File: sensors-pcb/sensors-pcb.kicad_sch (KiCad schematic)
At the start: 0 parts

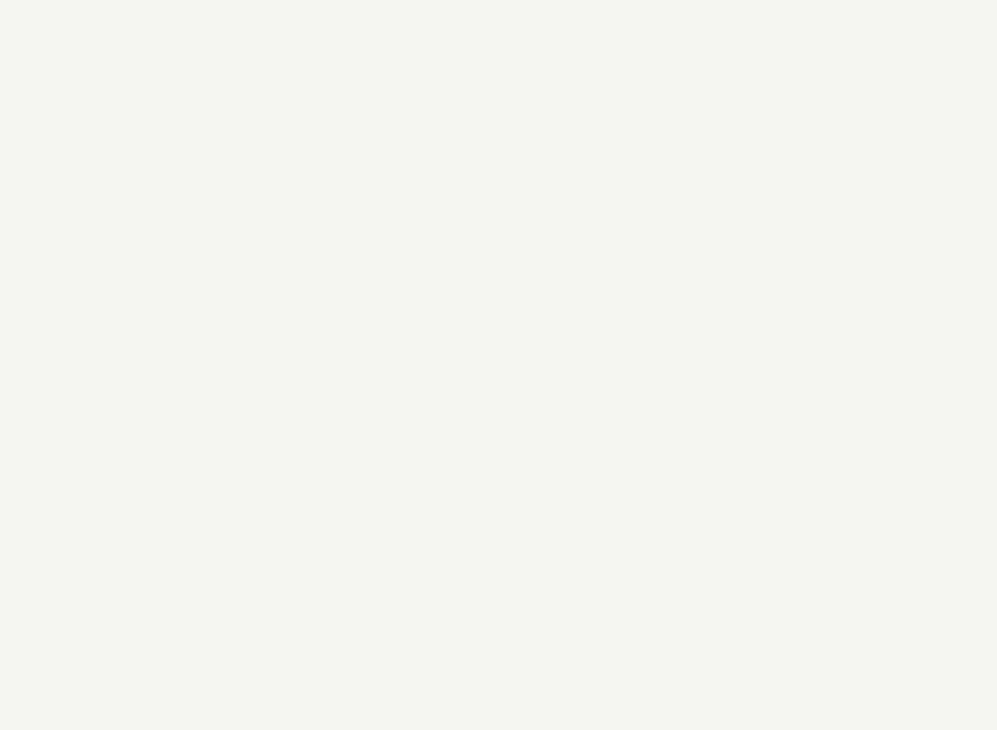
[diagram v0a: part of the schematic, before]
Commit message: Ajusté symbole IMU et commencé schéma
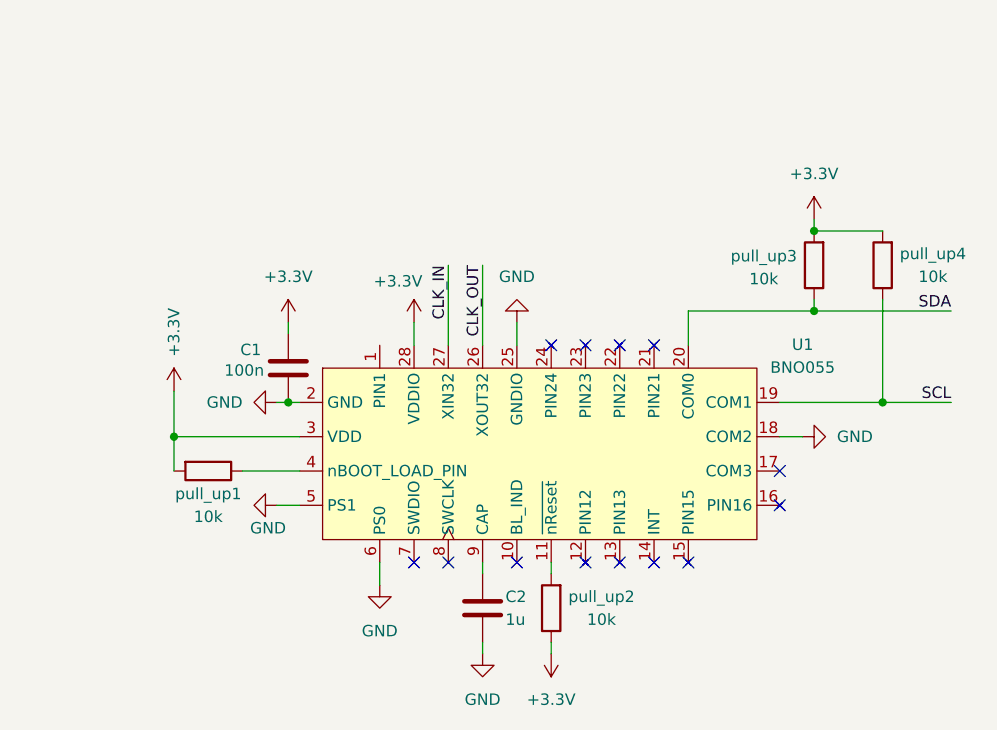
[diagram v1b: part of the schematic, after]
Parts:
- added C1: 100n, symbol Device:C
- added C2: 1u, symbol Device:C
- added U1: BNO055, symbol Exocet:BNO055
- added pull_up1, pull_up2, pull_up3, pull_up4: 10k, symbol Device:R
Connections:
- new net: C2.1, U1.9 (CAP)
- new net: U1.11 (~{nReset}), pull_up2.2
- new net: U1.4 (nBOOT_LOAD_PIN), pull_up1.1
- new net +3.3V: C1.2, U1.28 (VDDIO), U1.3 (VDD), pull_up1.2, pull_up2.1, pull_up3.2, pull_up4.2
- new net CLK_IN: U1.27 (XIN32)
- new net CLK_OUT: U1.26 (XOUT32)
- new net GND: C1.1, C2.2, U1.18 (COM2), U1.2 (GND), U1.25 (GNDIO), U1.5 (PS1), U1.6 (PS0)
- new net SCL: U1.19 (COM1), pull_up4.1
- new net SDA: U1.20 (COM0), pull_up3.1
- no-connect marks 0 -> 13

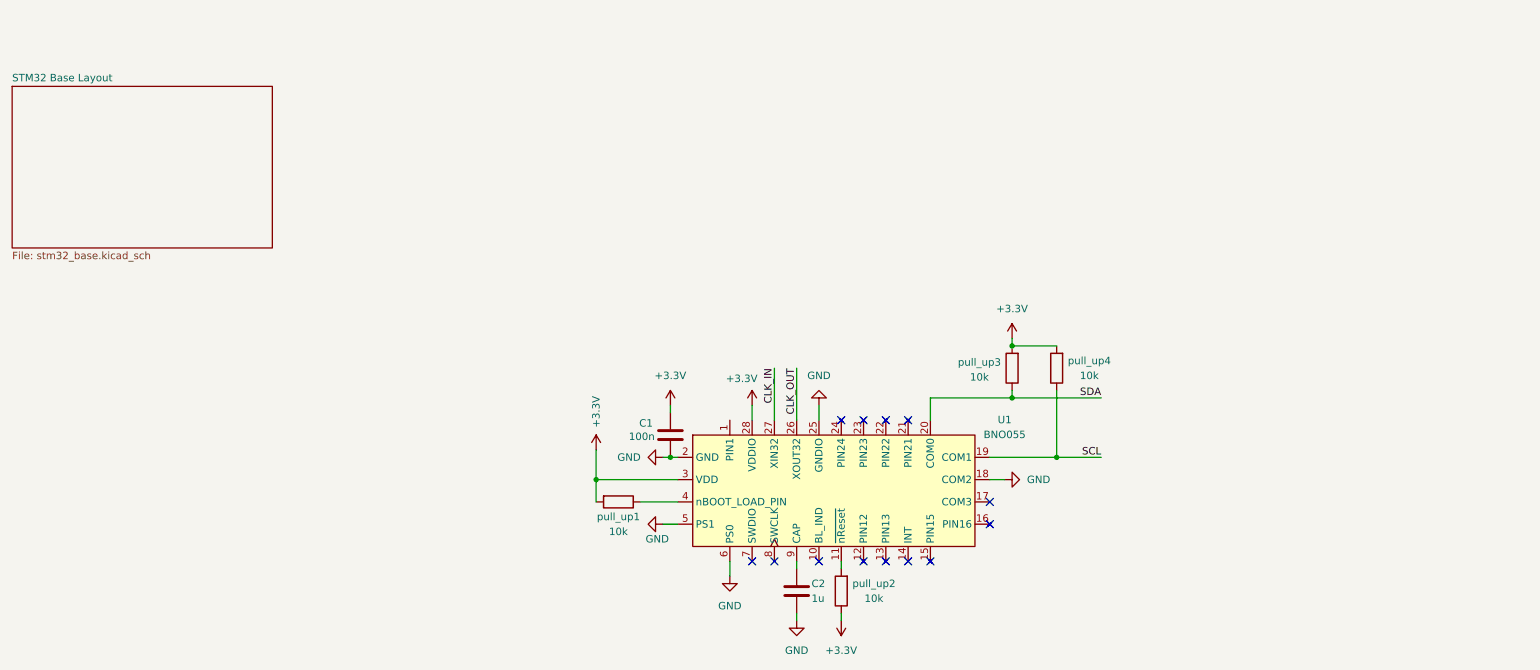
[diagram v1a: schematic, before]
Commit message: sensors-pcb: adjust IMU schematic and symbol
hide no connect pins
add connect I2C I/O to STM32 with pull-up resistors
add external 42kHz clock from Exocet template
pins 15 and 16 connected to GND through solder jumper
because of conflicting datasheet info (2021 vs 2016). to be tested IRL
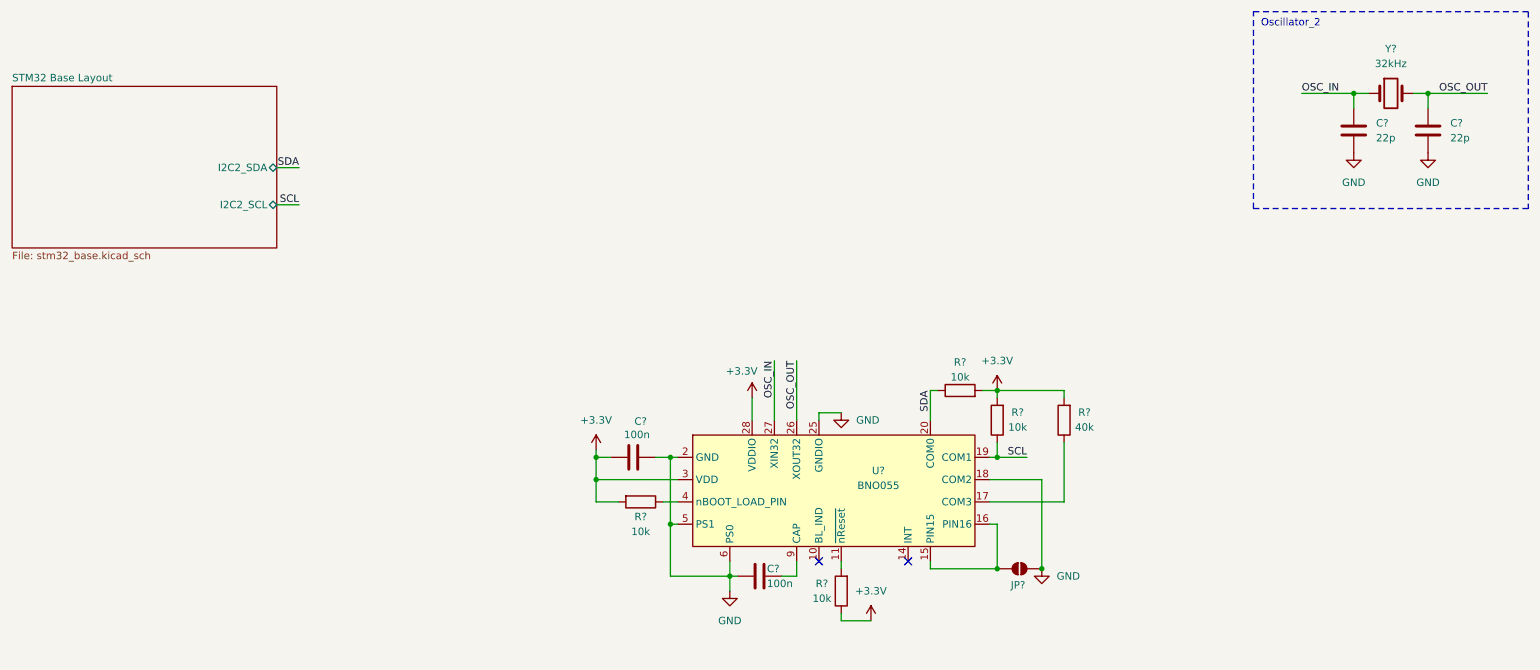
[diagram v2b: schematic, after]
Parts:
- removed pull_up3: 10k, symbol Device:R
- added C? (x2): 22p, Capacitor_SMD:C_0603_1608Metric, symbol Device:C
- added JP?: SolderJumper_2_Open, symbol Jumper:SolderJumper_2_Open
- added R?: 40k, symbol Device:R
- added R?: 10k, symbol Device:R
- added Y?: 32kHz, Exocet:Crystal_SMD_HC49-SD, symbol Exocet:HSE_Oscillator
- C?: renamed from C2; value 1u -> 100n
- renumbered C1 to C?, pull_up2 to R?, pull_up4 to R?, pull_up1 to R?, U1 to U?
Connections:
- net +3.3V: now also C?.1, R?.2, R?.2; no longer C?.2
- net GND: now also C?.2, C?.2, C?.2, JP?.2 (B); no longer C?.1
- net SDA: now also R?.1
- net at U?.15 (PIN15): now also U?.16 (PIN16), JP?.1 (A)
- net at U?.17 (COM3): now also R?.1
- net CLK_IN renamed OSC_IN
- net OSC_IN: now also C?.1, Y?.1
- net CLK_OUT renamed OSC_OUT
- net OSC_OUT: now also C?.1, Y?.2
- no-connect marks 13 -> 2
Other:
- sheet STM32 Base Layout ports: added I2C2_SCL, I2C2_SDA; removed none
- note added: "Oscillator_2"
- moved on the sheet: C?, R?

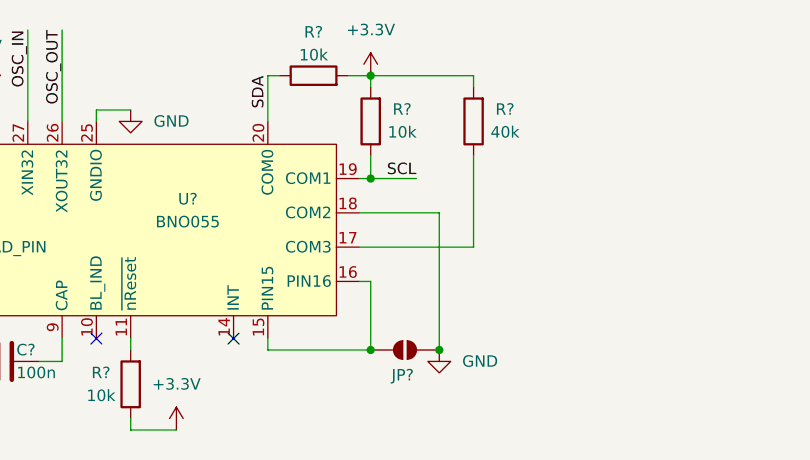
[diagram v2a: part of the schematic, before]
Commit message: sensors-pcb: add second solder junction
in case connecting pins together is illegal
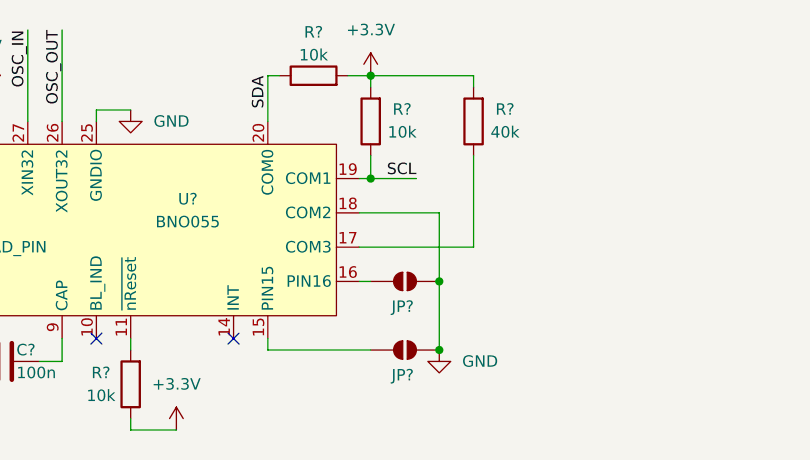
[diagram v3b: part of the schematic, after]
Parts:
- added JP?: SolderJumper_2_Open, symbol Jumper:SolderJumper_2_Open
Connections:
- net GND: now also JP?.2 (B)
- net at JP?.1 (A), U?.15 (PIN15): no longer U?.16 (PIN16)
- new net: JP?.1 (A), U?.16 (PIN16)
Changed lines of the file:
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@@
+	)
+	(junction
+		(at 200.66 100.33)
+		(diameter 0)
+		(color 0 0 0 0)
 	)
 	(junction
@@
 	(junction
 		(at 266.7 26.67)
-		(diameter 0)
-		(color 0 0 0 0)
-	)
-	(junction
-		(at 193.04 107.95)
 		(diameter 0)
 		(color 0 0 0 0)
@@
 	(wire
 		(pts
-			(xy 193.04 107.95) (xy 193.04 100.33)
-		)
-		(stroke
-			(width 0)
-			(type default)
-		)
-	)
-	(wire
-		(pts
 			(xy 147.32 109.22) (xy 147.32 111.76)
 		)
@@
 	(wire
 		(pts
+			(xy 200.66 100.33) (xy 200.66 107.95)
+		)
+		(stroke
+			(width 0)
+			(type default)
+		)
+	)
+	(wire
+		(pts
 			(xy 147.32 109.22) (xy 148.59 109.22)
 		)
@@
 	(wire
 		(pts
-			(xy 200.66 92.71) (xy 200.66 107.95)
+			(xy 200.66 92.71) (xy 200.66 100.33)
 		)
 		(stroke
@@
 					(unit 1)
 				)
+			)
+		)
+	)
+	(symbol
+		(lib_id "Jumper:SolderJumper_2_Open")
+		(at 196.85 100.33 0)
+		(unit 1)
+		(exclude_from_sim no)
+		(in_bom no)
+		(on_board yes)
+		(dnp no)
+		(property "Reference" "JP?"
+			(at 196.596 103.124 0)
+			(effects
+				(font
+					(size 1.27 1.27)
+				)
+			)
+		)
+		(property "Value" "SolderJumper_2_Open"
+			(at 196.596 105.664 0)
+			(effects
+				(font
+					(size 1.27 1.27)
+				)
+				(hide yes)
+			)
+		)
+		(property "Footprint" ""
+			(at 196.85 100.33 0)
+			(effects
+				(font
+					(size 1.27 1.27)
+				)
+				(hide yes)
+			)
+		)
+		(property "Datasheet" "~"
+			(at 196.85 100.33 0)
+			(effects
+				(font
+					(size 1.27 1.27)
+				)
+				(hide yes)
+			)
+		)
+		(property "Description" "Solder Jumper, 2-pole, open"
+			(at 196.85 100.33 0)
+			(effects
+				(font
+					(size 1.27 1.27)
+				)
+				(hide yes)
+			)
+		)
+		(pin "1"
+		)
+		(pin "2"
+		)
+		(instances
+			(project "sensors-pcb"
+				(path "/4b4cf3aa-c94c-4150-b9c5-35049cd71136"
+					(reference "JP?")
+					(unit 1)
+				)

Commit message: Symbole GPS
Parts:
- added AE1: Antenna, symbol Device:Antenna
- added R1, R2: 10k, symbol Device:R
- added R3: 50, symbol Device:R
- added U1: MAX-M8Q, RF_GPS:ublox_MAX, symbol RF_GPS:MAX-M8Q
- added V1: VPULSE, symbol Simulation_SPICE:VPULSE
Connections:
- net +3.3V: now also U1.14 (VCC_RF), U1.6 (V_BCKP), U1.7 (VCC_IO), U1.8 (VCC)
- net GND: now also U1.1 (GND), U1.10 (GND), U1.12 (GND), V1.2
- new net: AE1.1 (A), R3.1
- new net: U1.4 (TIMEPULSE), V1.1
- new net: R3.2, U1.11 (RF_IN)
- new net: R1.2, U1.16 (SDA)
- new net: R2.2, U1.17 (SCL)

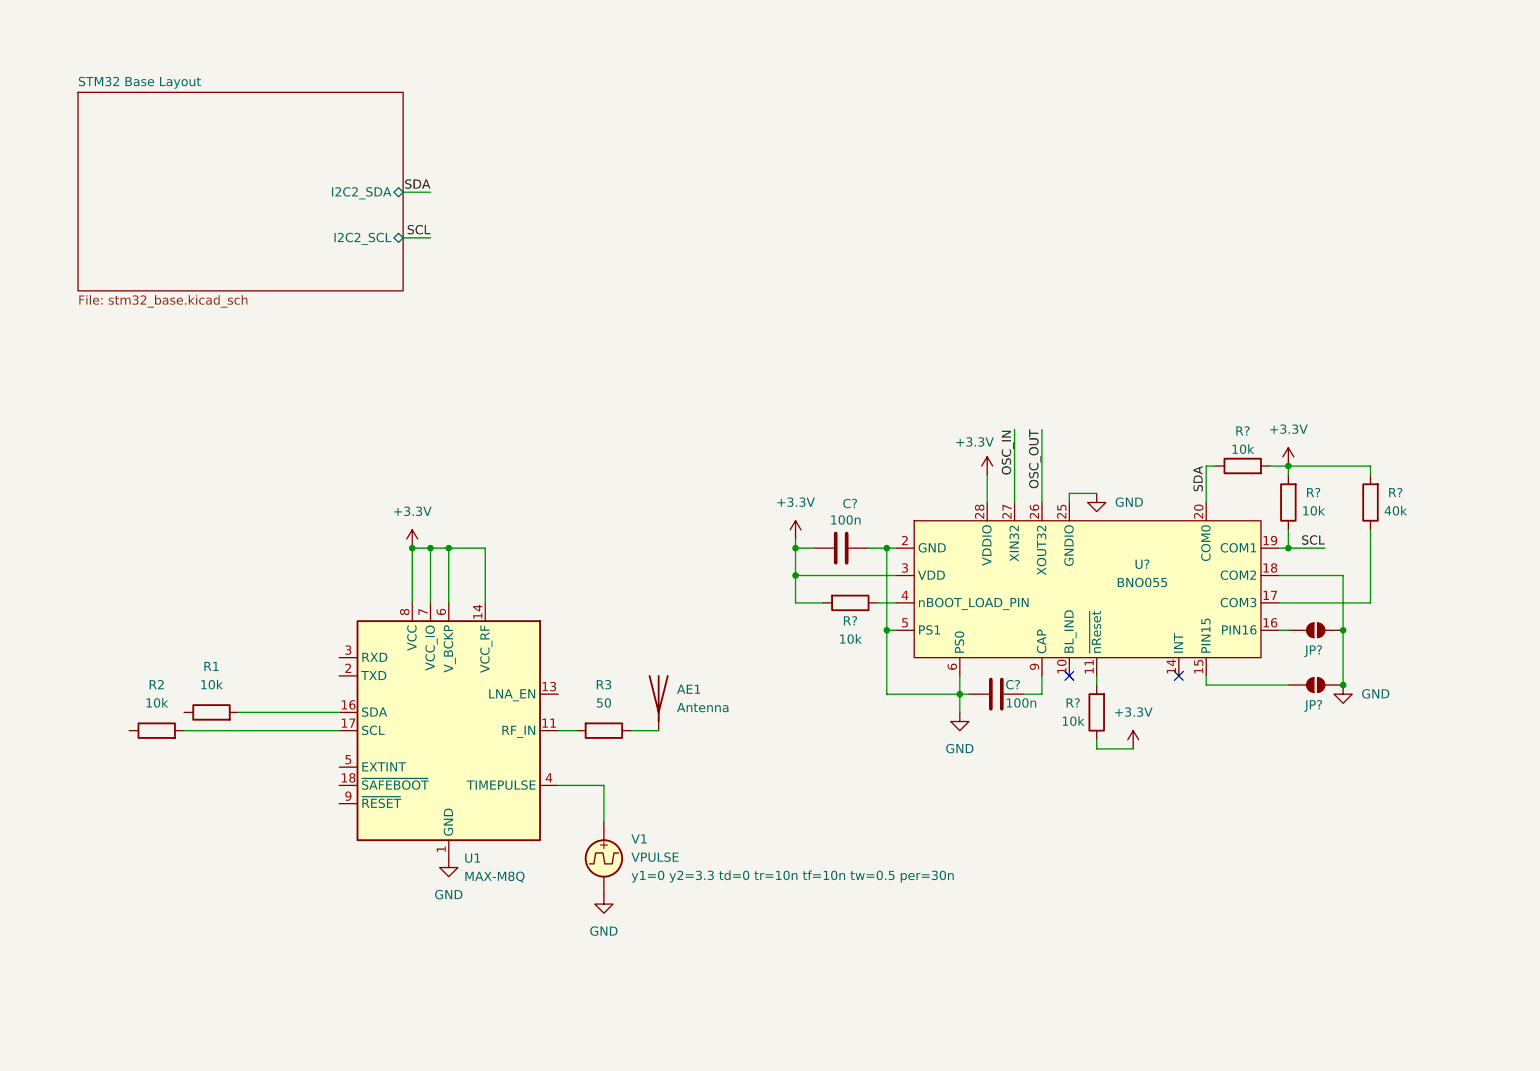
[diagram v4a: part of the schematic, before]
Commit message: sensors-pcb: finish GPS schematic
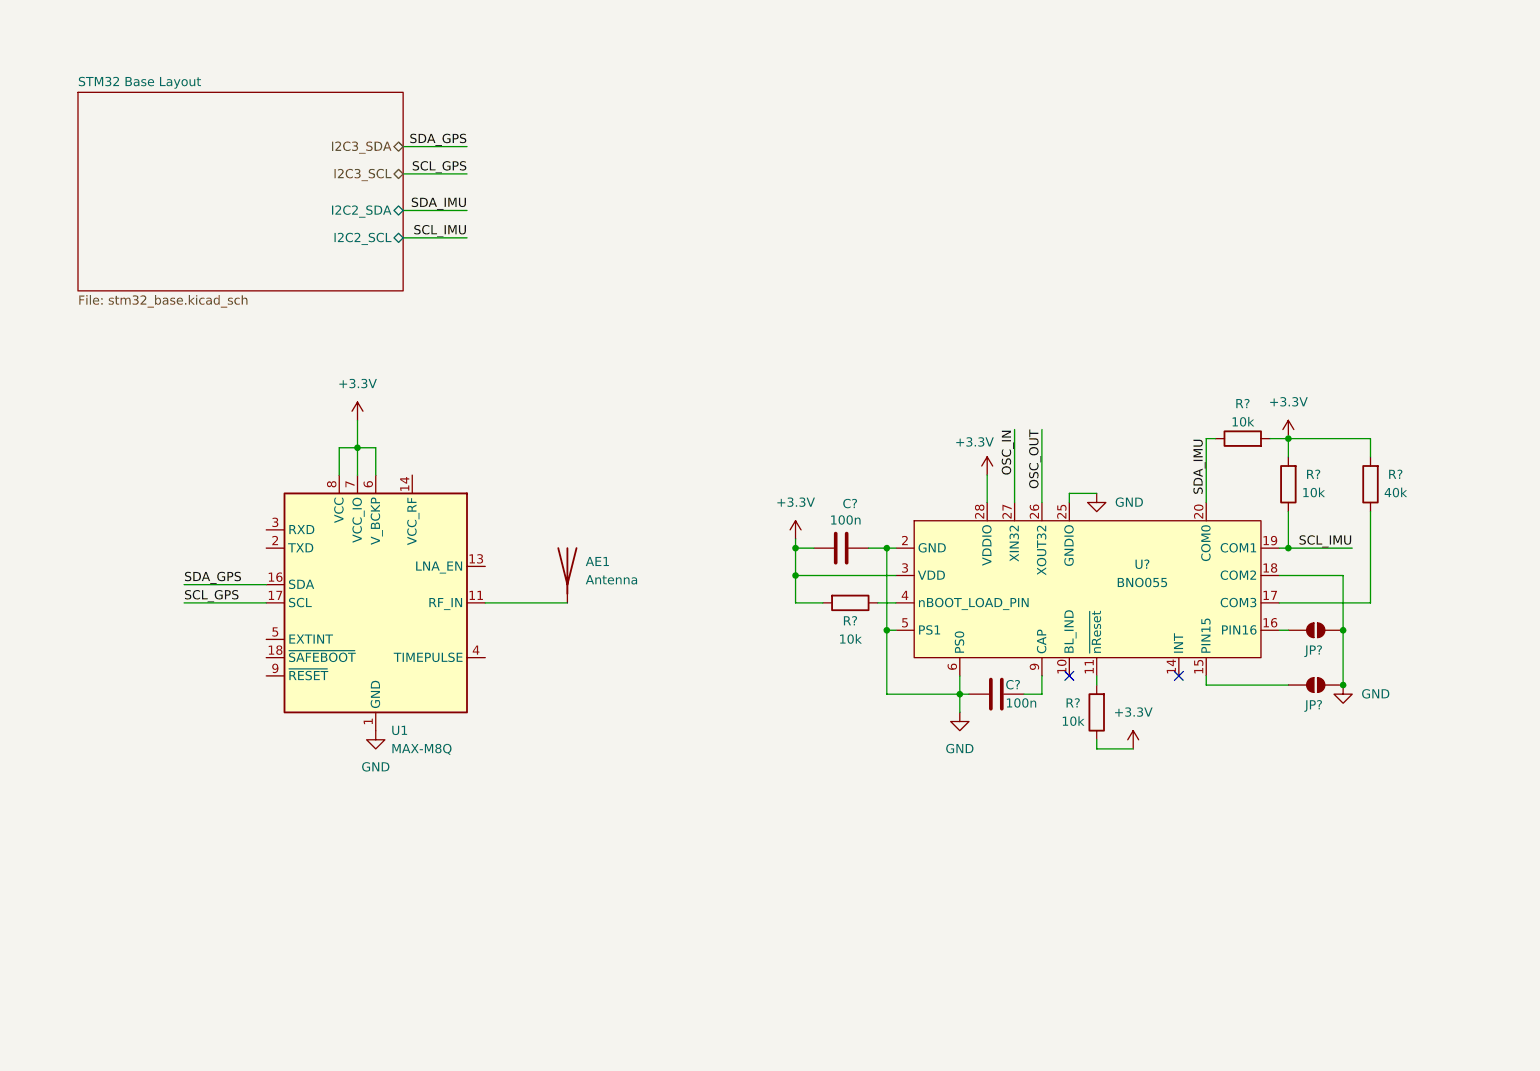
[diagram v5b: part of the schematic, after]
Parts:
- removed R1, R2: 10k, symbol Device:R
- removed R3: 50, symbol Device:R
- removed V1: VPULSE, symbol Simulation_SPICE:VPULSE
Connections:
- net +3.3V: no longer U1.14 (VCC_RF)
- net at AE1.1 (A): now also U1.11 (RF_IN)
- net I2C3_SDA: now reaches U1.16 (SDA)
- net I2C3_SCL: now reaches U1.17 (SCL)
- net SCL renamed SCL_IMU
- net SDA renamed SDA_IMU
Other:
- moved on the sheet: AE1, R?, U1
